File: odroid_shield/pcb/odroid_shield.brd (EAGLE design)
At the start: 83 x 48 mm, 71 parts, among them J1 AVRISP6_COMPACT, J4 ODROID_J4, U1 SINGLE-BIT_BUS_TRANSCEIVER, U10 ABM8G, U2 SINGLE-BIT_BUS_TRANSCEIVER, U3 ST1S10, U4 ATMEGA644P-20AU, U5 TS5205, U6 TCA9517MSOP8, U7 MC33926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

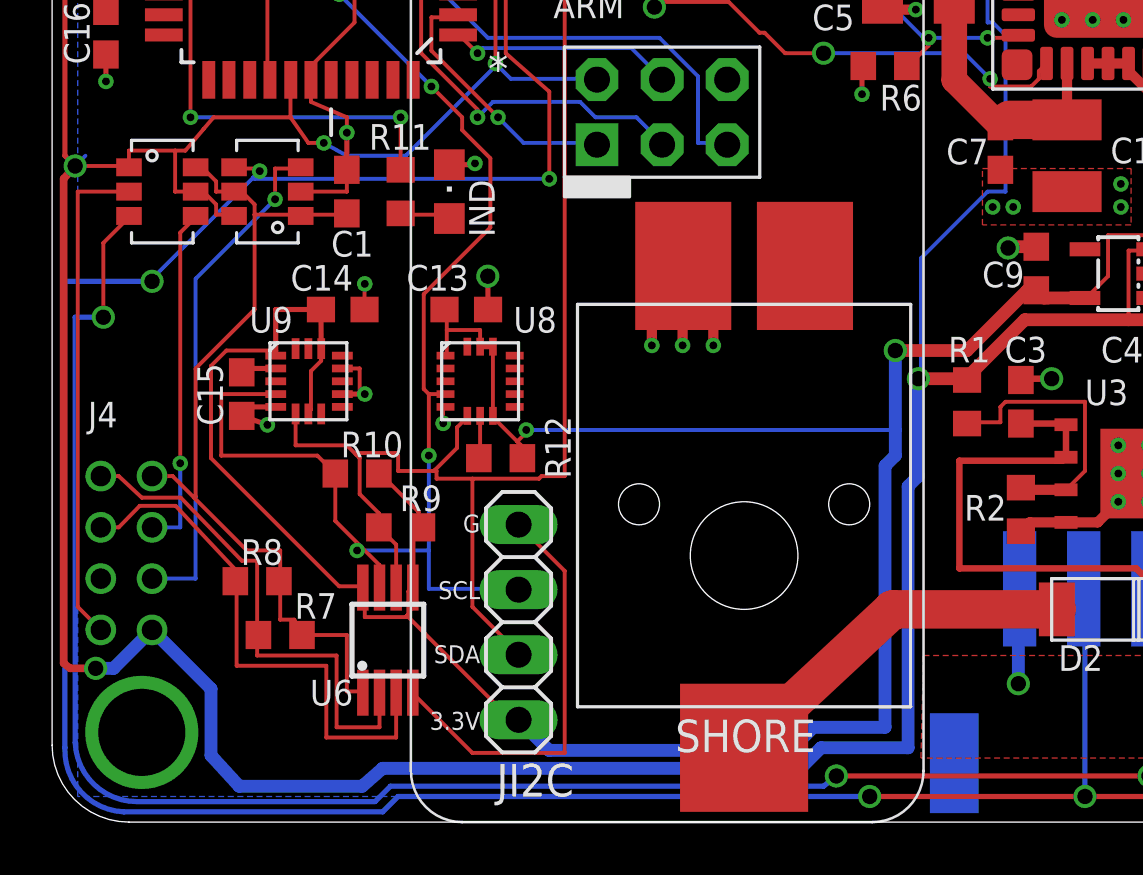
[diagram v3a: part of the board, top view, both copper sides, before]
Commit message: odroid_shield: Make the ground plane more contiguous.
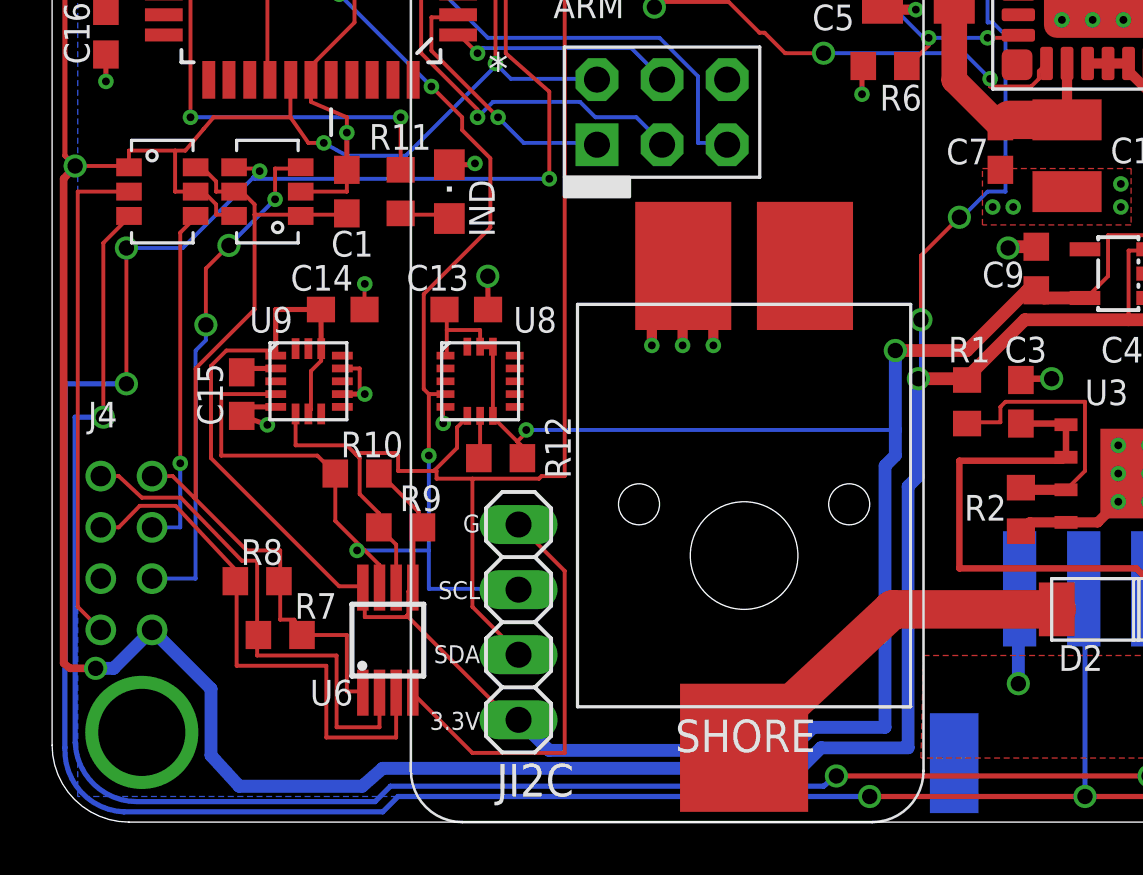
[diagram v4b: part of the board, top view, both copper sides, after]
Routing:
- net ODROID_TX_5V: track 273.2 -> 274.3 mm, vias 9 -> 10
- net +5V: track 227.4 -> 226.9 mm, vias 7 -> 9
- net N$4: vias 1 -> 3
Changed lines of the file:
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@@
 <layer number="44" name="Drills" color="7" fill="1" visible="no" active="yes"/>
 <layer number="45" name="Holes" color="7" fill="1" visible="no" active="yes"/>
-<layer number="46" name="Milling" color="3" fill="1" visible="no" active="yes"/>
+<layer number="46" name="Milling" color="3" fill="1" visible="yes" active="yes"/>
 <layer number="47" name="Measures" color="7" fill="1" visible="no" active="yes"/>
 <layer number="48" name="Document" color="7" fill="1" visible="yes" active="yes"/>
@@
 <layer number="98" name="Guide" color="6" fill="1" visible="no" active="no"/>
 <layer number="99" name="SpiceOrder" color="7" fill="1" visible="no" active="no"/>
-<layer number="100" name="help" color="7" fill="1" visible="yes" active="yes"/>
-<layer number="101" name="DOC" color="7" fill="1" visible="yes" active="yes"/>
-<layer number="102" name="bot_pads" color="7" fill="1" visible="yes" active="yes"/>
+<layer number="100" name="help" color="7" fill="1" visible="no" active="yes"/>
+<layer number="101" name="DOC" color="7" fill="1" visible="no" active="yes"/>
+<layer number="102" name="bot_pads" color="7" fill="1" visible="no" active="yes"/>
 <layer number="103" name="tMap" color="7" fill="1" visible="no" active="yes"/>
-<layer number="104" name="S_DOKU" color="7" fill="1" visible="yes" active="yes"/>
+<layer number="104" name="S_DOKU" color="7" fill="1" visible="no" active="yes"/>
 <layer number="105" name="tPlate" color="7" fill="1" visible="no" active="yes"/>
 <layer number="106" name="bPlate" color="7" fill="1" visible="no" active="yes"/>
 <layer number="107" name="Crop" color="7" fill="1" visible="no" active="yes"/>
-<layer number="108" name="tplace-old" color="10" fill="1" visible="yes" active="yes"/>
-<layer number="109" name="ref-old" color="11" fill="1" visible="yes" active="yes"/>
-<layer number="111" name="tGTest" color="7" fill="1" visible="yes" active="yes"/>
-<layer number="112" name="bGTest" color="7" fill="1" visible="yes" active="yes"/>
-<layer number="116" name="Patch_BOT" color="7" fill="1" visible="yes" active="yes"/>
+<layer number="108" name="tplace-old" color="10" fill="1" visible="no" active="yes"/>
+<layer number="109" name="ref-old" color="11" fill="1" visible="no" active="yes"/>
+<layer number="111" name="tGTest" color="7" fill="1" visible="no" active="yes"/>
+<layer number="112" name="bGTest" color="7" fill="1" visible="no" active="yes"/>
+<layer number="116" name="Patch_BOT" color="7" fill="1" visible="no" active="yes"/>
 <layer number="121" name="_tsilk" color="7" fill="1" visible="no" active="yes"/>
 <layer number="122" name="_bsilk" color="7" fill="1" visible="no" active="yes"/>
 <layer number="125" name="_tNames" color="7" fill="1" visible="no" active="yes"/>
 <layer number="144" name="Drill_legend" color="7" fill="1" visible="no" active="yes"/>
-<layer number="150" name="Notes" color="7" fill="1" visible="yes" active="yes"/>
+<layer number="150" name="Notes" color="7" fill="1" visible="no" active="yes"/>
 <layer number="151" name="HeatSink" color="7" fill="1" visible="no" active="yes"/>
-<layer number="199" name="Contour" color="7" fill="1" visible="yes" active="yes"/>
+<layer number="199" name="Contour" color="7" fill="1" visible="no" active="yes"/>
 <layer number="200" name="200bmp" color="15" fill="1" visible="no" active="yes"/>
 <layer number="201" name="201bmp" color="2" fill="10" visible="no" active="yes"/>
@@
 <layer number="250" name="Descript" color="3" fill="1" visible="no" active="no"/>
 <layer number="251" name="SMDround" color="12" fill="11" visible="no" active="no"/>
-<layer number="254" name="OrgLBR" color="7" fill="1" visible="yes" active="yes"/>
+<layer number="254" name="OrgLBR" color="7" fill="1" visible="no" active="yes"/>
 </layers>
 <board>
@@
 <wire x1="37.2" y1="24.6" x2="37.2" y2="30.7" width="0.1524" layer="16"/>
 <wire x1="36.5" y1="24.6" x2="37.2" y2="24.6" width="0.1524" layer="16"/>
-<wire x1="33.9" y1="22" x2="36.5" y2="24.6" width="0.1524" layer="16"/>
-<wire x1="33.9" y1="17.5" x2="33.9" y2="22" width="0.1524" layer="16"/>
 <wire x1="33.9" y1="17.5" x2="33.8" y2="17.3" width="0.1524" layer="16"/>
 <wire x1="2.1" y1="35.5" x2="4.3" y2="35.5" width="0.1524" layer="1"/>
@@
 <wire x1="10" y1="44.3" x2="15.69" y2="44.3" width="0.1524" layer="16"/>
 <wire x1="13.8" y1="26" x2="17.3" y2="29.5" width="0.1524" layer="16"/>
-<wire x1="0.9" y1="25.6" x2="1.3" y2="26" width="0.1524" layer="16"/>
 <wire x1="17.3" y1="29.5" x2="17.3" y2="29.6" width="0.1524" layer="16"/>
 <via x="17.3" y="29.6" extent="1-16" drill="0.3048"/>
@@
 <wire x1="10.6" y1="26.5" x2="10" y2="26.5" width="0.1524" layer="1"/>
 <wire x1="10" y1="26.5" x2="9.3" y2="27.5" width="0.1524" layer="1"/>
+<wire x1="33.9" y1="17.5" x2="33.9" y2="19.6" width="0.1524" layer="16"/>
+<via x="33.9" y="19.6" extent="1-16" drill="0.6"/>
+<wire x1="33.9" y1="19.6" x2="33.9" y2="22.1" width="0.1524" layer="1"/>
+<wire x1="33.9" y1="22.1" x2="35.4" y2="23.6" width="0.1524" layer="1"/>
+<via x="35.4" y="23.6" extent="1-16" drill="0.6"/>
+<wire x1="35.4" y1="23.6" x2="35.5" y2="23.6" width="0.1524" layer="16"/>
+<wire x1="35.5" y1="23.6" x2="36.5" y2="24.6" width="0.1524" layer="16"/>
 </signal>
 <signal name="GND">
@@
 <wire x1="12.6" y1="0.8" x2="3.3" y2="0.8" width="0.2032" layer="16"/>
 <wire x1="3.3" y1="0.8" x2="0.9" y2="3.1" width="0.2032" layer="16" curve="-87.562224"/>
-<wire x1="0.9" y1="3.1" x2="0.9" y2="19.7" width="0.2032" layer="16"/>
-<wire x1="0.9" y1="19.7" x2="2" y2="19.7" width="0.2032" layer="16"/>
-<via x="2" y="19.7" extent="1-16" drill="0.6"/>
+<wire x1="0.9" y1="3.1" x2="0.9" y2="15.8" width="0.2032" layer="16"/>
+<wire x1="0.9" y1="15.8" x2="2" y2="15.8" width="0.2032" layer="16"/>
+<via x="2" y="15.8" extent="1-16" drill="0.6"/>
 <wire x1="2" y1="22.6" x2="3" y2="23.6" width="0.1524" layer="1"/>
-<wire x1="2" y1="19.7" x2="2" y2="22.6" width="0.1524" layer="1"/>
+<wire x1="2" y1="15.8" x2="2" y2="22.6" width="0.1524" layer="1"/>
 <wire x1="3" y1="23.6" x2="3" y2="23.65" width="0.1524" layer="1"/>
 <wire x1="22.1" y1="38" x2="15.9" y2="38" width="0.1524" layer="1"/>
@@
 <wire x1="8.7" y1="25.5" x2="9.7" y2="25.5" width="0.1524" layer="1"/>
 <wire x1="8.7" y1="24.3" x2="8.7" y2="25.5" width="0.1524" layer="1"/>
-<wire x1="5.6" y1="21.2" x2="8.7" y2="24.3" width="0.1524" layer="16"/>
-<wire x1="5.6" y1="9.5" x2="5.6" y2="21.2" width="0.1524" layer="16"/>
 <wire x1="3.9" y1="9.5" x2="5.6" y2="9.5" width="0.1524" layer="16"/>
 <wire x1="9.7" y1="25.5" x2="9.7" y2="25.55" width="0.1524" layer="1"/>
 <via x="8.7" y="24.3" extent="1-16" drill="0.3048"/>
+<wire x1="8.7" y1="24.3" x2="6.9" y2="22.5" width="0.1524" layer="16"/>
+<via x="6.9" y="22.5" extent="1-16" drill="0.6"/>
+<wire x1="6.9" y1="22.5" x2="6" y2="21.6" width="0.1524" layer="1"/>
+<wire x1="6" y1="21.6" x2="6" y2="19.4" width="0.1524" layer="1"/>
+<via x="6" y="19.4" extent="1-16" drill="0.6"/>
+<wire x1="6" y1="19.4" x2="6" y2="18.8" width="0.1524" layer="16"/>
+<wire x1="6" y1="18.8" x2="5.6" y2="18.4" width="0.1524" layer="16"/>
+<wire x1="5.6" y1="18.4" x2="5.6" y2="9.5" width="0.1524" layer="16"/>
 </signal>
 <signal name="ODROID_TX_5V">
@@
 <wire x1="12.9" y1="0.4" x2="2.8" y2="0.4" width="0.2032" layer="16"/>
 <wire x1="2.8" y1="0.4" x2="0.5" y2="2.9" width="0.2032" layer="16" curve="-90"/>
-<wire x1="0.5" y1="2.9" x2="0.5" y2="21.1" width="0.2032" layer="16"/>
-<wire x1="0.5" y1="21.1" x2="3.9" y2="21.1" width="0.2032" layer="16"/>
-<via x="3.9" y="21.1" extent="1-16" drill="0.6"/>
+<wire x1="0.5" y1="2.9" x2="0.5" y2="17.1" width="0.2032" layer="16"/>
+<wire x1="0.5" y1="17.1" x2="2.9" y2="17.1" width="0.2032" layer="16"/>
+<via x="2.9" y="17.1" extent="1-16" drill="0.6"/>
 <wire x1="8.1" y1="25.5" x2="7.1" y2="25.5" width="0.1524" layer="1"/>
 <wire x1="8.1" y1="25.4" x2="8.1" y2="25.5" width="0.1524" layer="1"/>
-<wire x1="3.9" y1="21.2" x2="7.85" y2="25.15" width="0.1524" layer="16"/>
 <wire x1="7.85" y1="25.15" x2="8.1" y2="25.4" width="0.1524" layer="16"/>
 <wire x1="7.1" y1="25.5" x2="7.1" y2="25.55" width="0.1524" layer="1"/>
-<wire x1="3.9" y1="21.2" x2="3.9" y2="21.1" width="0.1524" layer="16"/>
 <wire x1="17.7" y1="37.1" x2="15.9" y2="37.1" width="0.1524" layer="1"/>
 <wire x1="17.7" y1="30" x2="17.7" y2="37.1" width="0.1524" layer="1"/>
@@
 <via x="8.1" y="25.4" extent="1-16" drill="0.3048"/>
 <via x="19.4" y="25.1" extent="1-16" drill="0.3048"/>
+<wire x1="2.9" y1="17.1" x2="2.9" y2="22.4" width="0.1524" layer="1"/>
+<via x="2.9" y="22.4" extent="1-16" drill="0.6"/>
+<wire x1="2.9" y1="22.4" x2="5.1" y2="22.4" width="0.1524" layer="16"/>
+<wire x1="5.1" y1="22.4" x2="8.1" y2="25.4" width="0.1524" layer="16"/>
 </signal>
 <signal name="N$1">

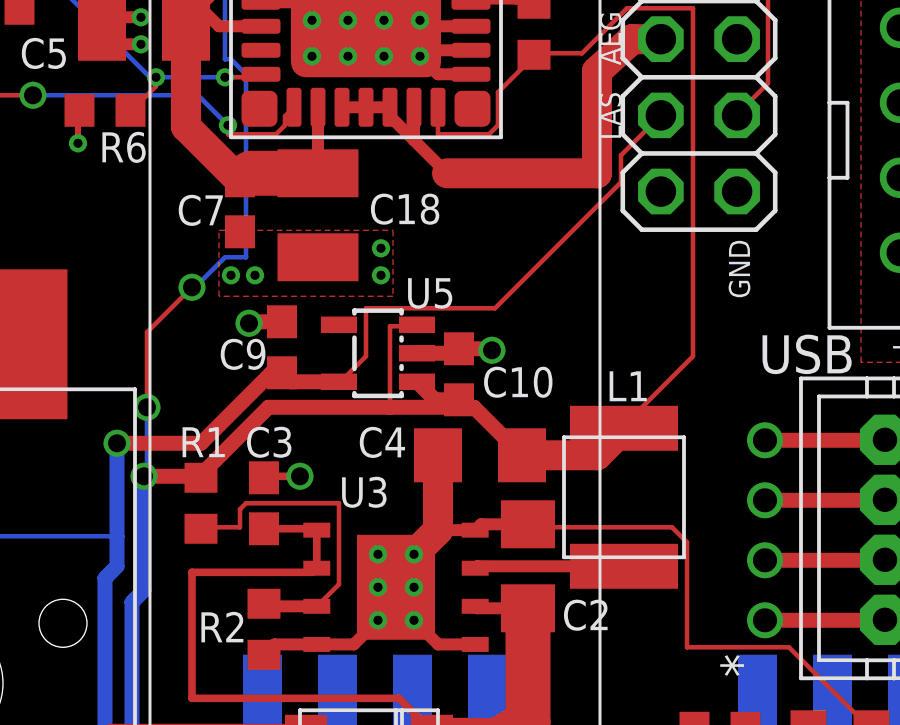
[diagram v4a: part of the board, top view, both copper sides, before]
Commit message: odroid_shield: Updates after pre-mfg checks from macrofab.
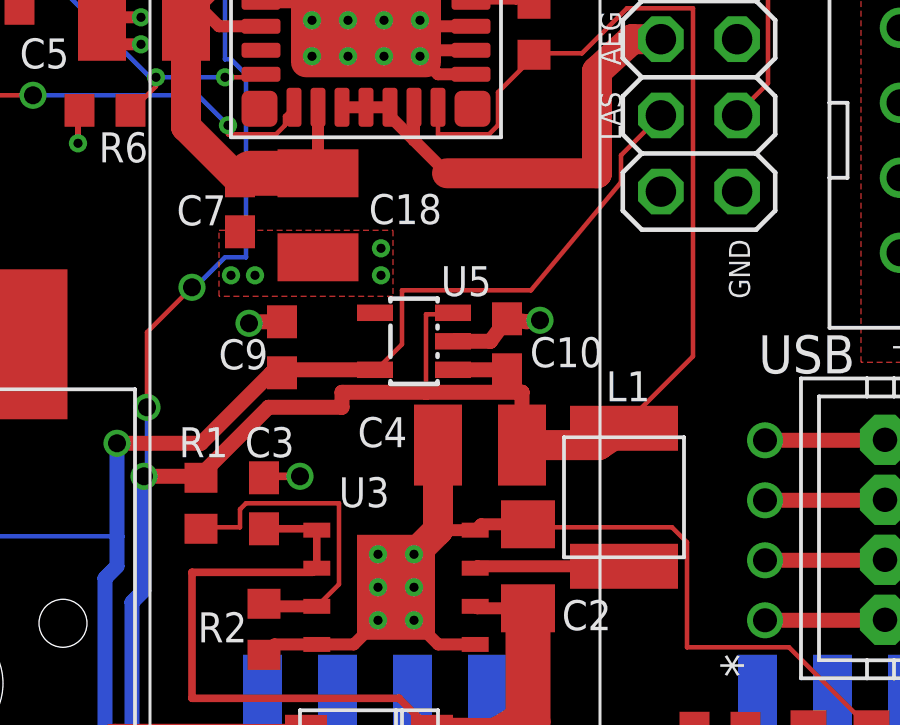
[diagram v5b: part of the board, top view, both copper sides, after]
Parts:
- C11, C12: value 20pF -> 22pF
- C4: device rcl:C1206 -> rcl:C1210
- L1: value 33uH -> 3.3uH
- R10, R7, R8, R9: value 4.7k -> 5.6k
- R11, R6: value 200 -> 220
- R3, R4: value 500 -> 560
- moved C10 1.89 mm to (45.9, 21.7)
- moved U5 1.26 mm to (42.8, 21.8)
- moved C4 0.34 mm to (45.0, 18.3)
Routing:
- net +5V: track 226.9 -> 229.2 mm
- net GND: track 138.3 -> 139.4 mm
